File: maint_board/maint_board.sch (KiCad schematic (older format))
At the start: 9 parts, among them J1 USB_mini_micro_B, J2 4P4C, J5 USB_C_Receptacle_USB2.0

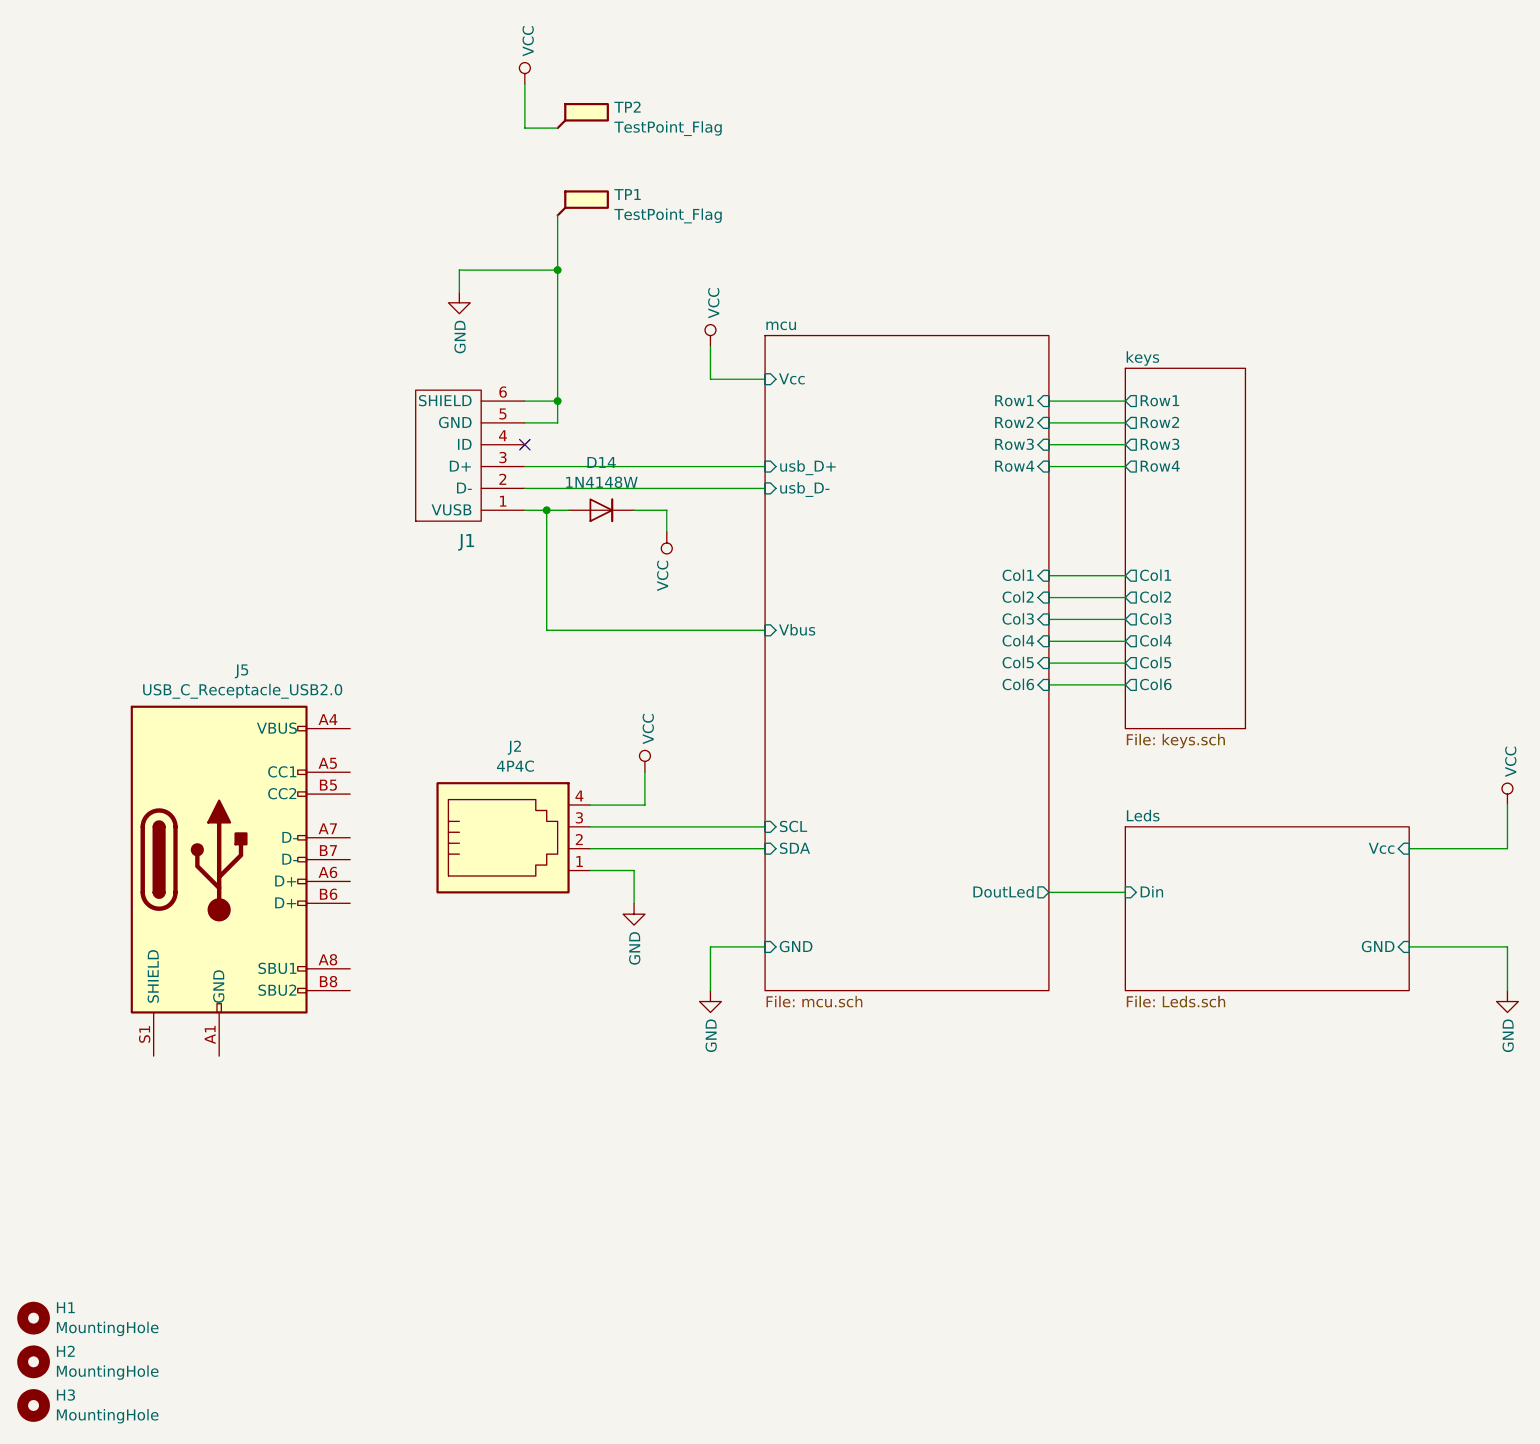
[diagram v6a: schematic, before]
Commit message: added filter on usb shield
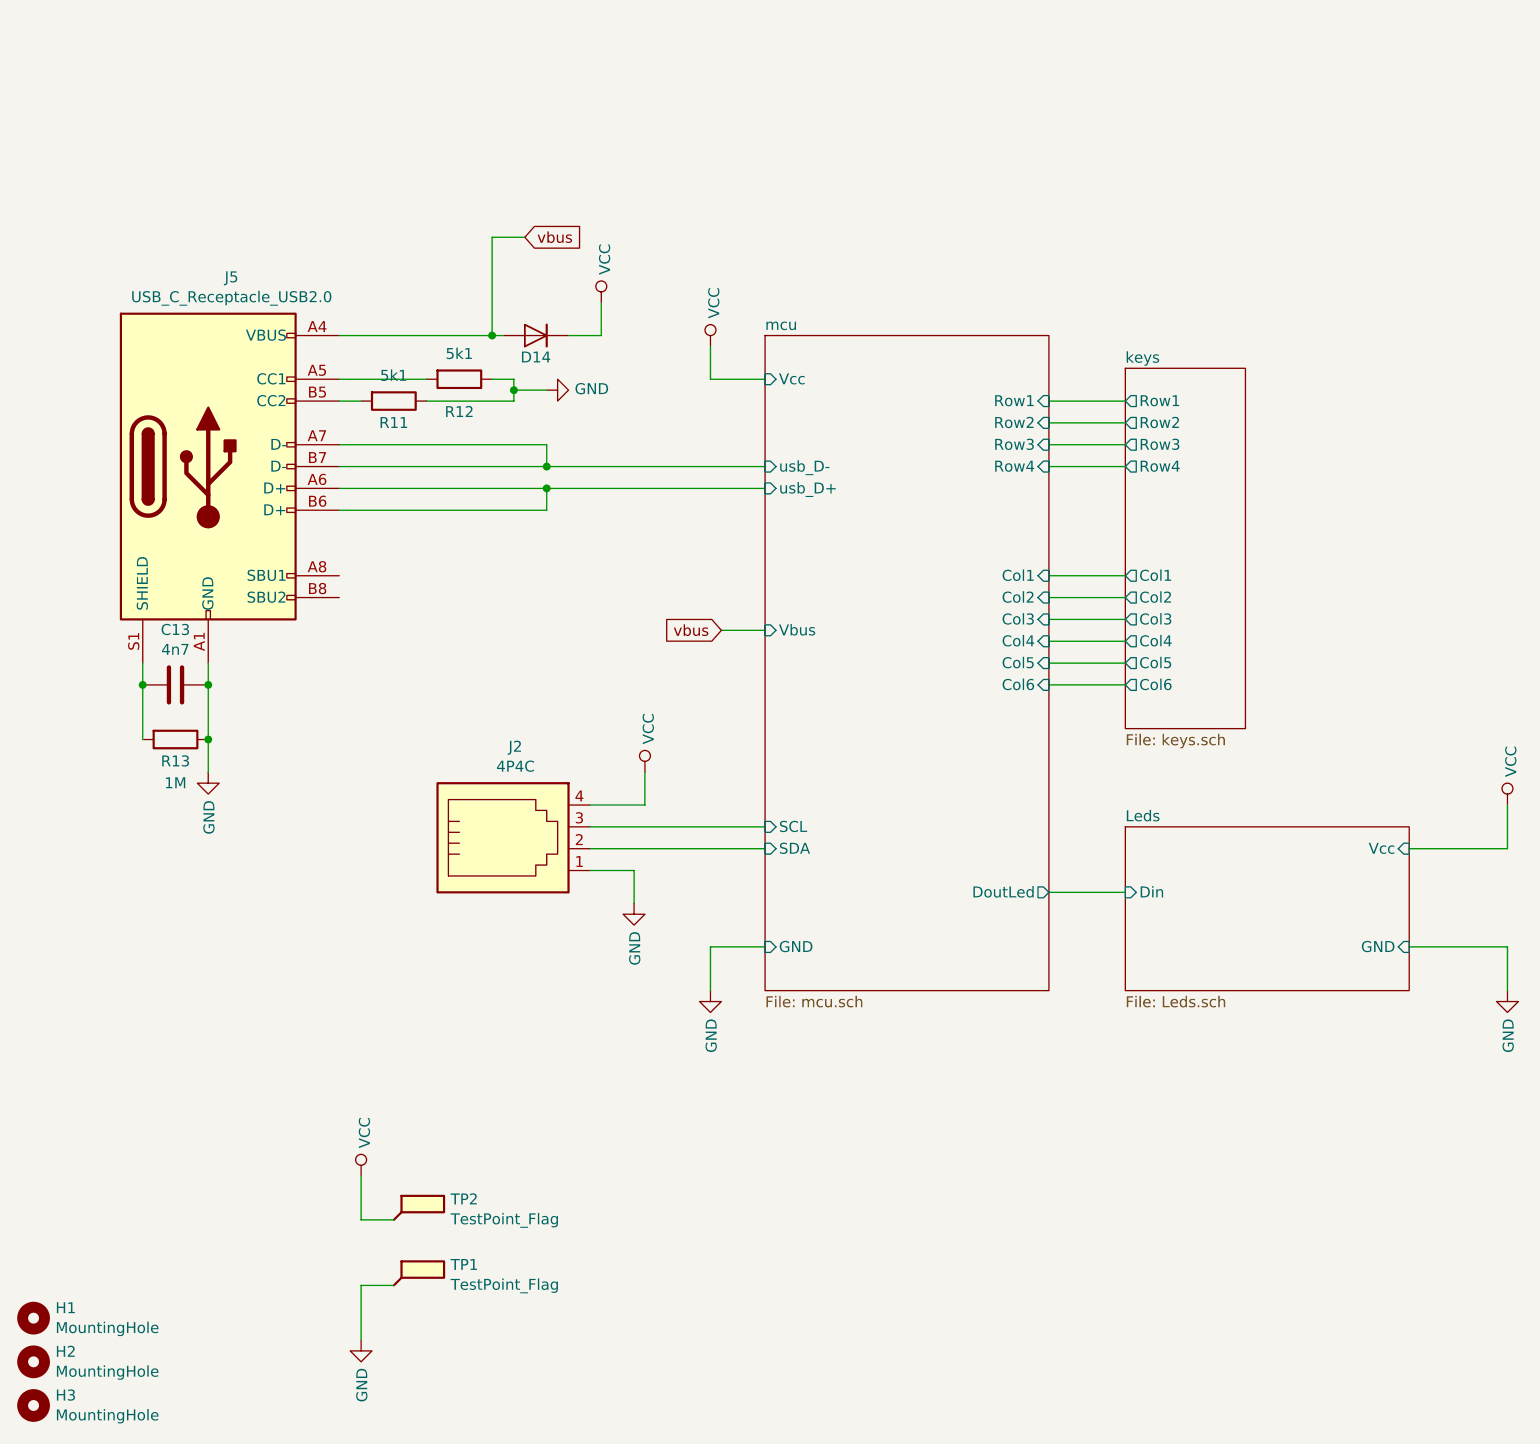
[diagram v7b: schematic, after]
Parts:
- removed J1: USB_mini_micro_B, TB_connectors:usb_minib_wm5462ct-nd, symbol maint_board-rescue:USB_mini_micro_B-keyboard_parts-maint_board-rescue
- added C13: 4n7, keyboard_parts:C_1608, symbol Device:C
- added R11, R12: 5k1, Resistor_SMD:R_0603_1608Metric_Pad1.05x0.95mm_HandSolder, symbol Device:R
- added R13: 1M, Resistor_SMD:R_0603_1608Metric_Pad1.05x0.95mm_HandSolder, symbol Device:R
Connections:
- net mcu/Vbus is gone; now on net vbus: D14.2 (A)
- net GND: now also J5.A1 (GND), J5.A12 (GND), J5.B1 (GND), J5.B12 (GND), C13.1, R11.1, R12.1, R13.1
- net mcu/usb_D+: now also J5.A6 (D+), J5.B6 (D+)
- net mcu/usb_D-: now also J5.A7 (D-), J5.B7 (D-)
- net vbus: now reaches J5.A4 (VBUS), J5.A9 (VBUS), J5.B4 (VBUS), J5.B9 (VBUS)
- net at J5.A5 (CC1): now also R12.2
- net at J5.B5 (CC2): now also R11.2
- net at J5.S1 (SHIELD): now also C13.2, R13.2
- no-connect marks 1 -> 0
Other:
- moved on the sheet: D14, J5, TP1, TP2
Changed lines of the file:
@@
 L power:GND #PWR013
 U 1 1 6050A70E
-P 3000 2250
-F 0 "#PWR013" H 3000 2000 50  0001 C CNN
-F 1 "GND" V 3005 2122 50  0000 R CNN
-F 2 "" H 3000 2250 50  0001 C CNN
-F 3 "" H 3000 2250 50  0001 C CNN
-	1    3000 2250
+P 1850 4450
+F 0 "#PWR013" H 1850 4200 50  0001 C CNN
+F 1 "GND" V 1855 4322 50  0000 R CNN
+F 2 "" H 1850 4450 50  0001 C CNN
+F 3 "" H 1850 4450 50  0001 C CNN
+	1    1850 4450
 	1    0    0    -1
 $EndComp
@@
 L power:VCC #PWR03
 U 1 1 601B611E
-P 3950 3350
-F 0 "#PWR03" H 3950 3200 50  0001 C CNN
-F 1 "VCC" V 3967 3478 50  0000 L CNN
-F 2 "" H 3950 3350 50  0001 C CNN
-F 3 "" H 3950 3350 50  0001 C CNN
-	1    3950 3350
-	-1   0    0    1
-$EndComp
-Wire Wire Line
-	3300 3250 3400 3250
-Wire Wire Line
-	3950 3350 3950 3250
-Wire Wire Line
-	3300 2750 3450 2750
-NoConn ~ 3300 2950
+P 3650 2300
+F 0 "#PWR03" H 3650 2150 50  0001 C CNN
+F 1 "VCC" V 3667 2428 50  0000 L CNN
+F 2 "" H 3650 2300 50  0001 C CNN
+F 3 "" H 3650 2300 50  0001 C CNN
+	1    3650 2300
+	1    0    0    -1
+$EndComp
 Wire Wire Line
 	6050 2750 5700 2750
@@
 F4 "Din" I L 6050 5000 50
 $EndSheet
-Wire Wire Line
-	3300 3050 4400 3050
-Wire Wire Line
-	4400 3150 3300 3150
 $Comp
 L power:VCC #PWR06
@@
 Wire Wire Line
 	5700 5000 6050 5000
-$Comp
-L maint_board-rescue:USB_mini_micro_B-keyboard_parts-maint_board-rescue J1
-U 1 1 601E1AA5
-P 3150 3100
-F 0 "J1" H 3037 3391 60  0000 C CNN
-F 1 "USB_mini_micro_B" H 3000 3350 60  0001 C CNN
-F 2 "TB_connectors:usb_minib_wm5462ct-nd" H 3100 3100 60  0001 C CNN
-F 3 "" H 3100 3100 60  0000 C CNN
-	1    3150 3100
-	1    0    0    1
-$EndComp
-Wire Wire Line
-	3450 2750 3450 2150
-Wire Wire Line
-	3450 2150 3000 2150
-Wire Wire Line
-	3000 2150 3000 2250
-Wire Wire Line
-	3300 2850 3450 2850
-Wire Wire Line
-	3450 2850 3450 2750
-Connection ~ 3450 2750
-Wire Wire Line
-	3800 3250 3950 3250
-Wire Wire Line
-	3400 3250 3400 3800
-Connection ~ 3400 3250
-Wire Wire Line
-	3400 3250 3500 3250
+Wire Wire Line
+	3500 2450 3650 2450
 $Sheet
 S 4400 2450 1300 3000
@@
 F10 "Col5" I R 5700 3950 50
 F11 "Col6" I R 5700 4050 50
-F12 "usb_D-" I L 4400 3150 50
-F13 "usb_D+" I L 4400 3050 50
+F12 "usb_D-" I L 4400 3050 50
+F13 "usb_D+" I L 4400 3150 50
 F14 "Vcc" I L 4400 2650 50
 F15 "GND" I L 4400 5250 50
@@
 $EndSheet
 Wire Wire Line
-	3400 3800 4400 3800
+	4200 3800 4400 3800
 $Comp
 L Diode:1N4148W D14
 U 1 1 61967A26
-P 3650 3250
-F 0 "D14" H 3650 3033 50  0000 C CNN
-F 1 "1N4148W" H 3650 3124 50  0000 C CNN
-F 2 "Diode_SMD:D_SOD-323" H 3650 3075 50  0001 C CNN
-F 3 "https://www.vishay.com/docs/85748/1n4148w.pdf" H 3650 3250 50  0001 C CNN
-	1    3650 3250
+P 3350 2450
+F 0 "D14" H 3350 2550 50  0000 C CNN
+F 1 "1N4148W" H 3350 2700 50  0001 C CNN
+F 2 "Diode_SMD:D_SOD-323" H 3350 2275 50  0001 C CNN
+F 3 "https://www.vishay.com/docs/85748/1n4148w.pdf" H 3350 2450 50  0001 C CNN
+	1    3350 2450
 	-1   0    0    1
 $EndComp
@@
 L Connector:TestPoint_Flag TP1
 U 1 1 61949AE4
-P 3450 1900
-F 0 "TP1" H 3710 1994 50  0000 L CNN
-F 1 "TestPoint_Flag" H 3710 1903 50  0000 L CNN
-F 2 "TestPoint:TestPoint_Pad_1.5x1.5mm" H 3650 1900 50  0001 C CNN
-F 3 "~" H 3650 1900 50  0001 C CNN
-	1    3450 1900
-	1    0    0    -1
-$EndComp
-Wire Wire Line
-	3450 1900 3450 2150
-Connection ~ 3450 2150
+P 2700 6800
+F 0 "TP1" H 2960 6894 50  0000 L CNN
+F 1 "TestPoint_Flag" H 2960 6803 50  0000 L CNN
+F 2 "TestPoint:TestPoint_Pad_1.5x1.5mm" H 2900 6800 50  0001 C CNN
+F 3 "~" H 2900 6800 50  0001 C CNN
+	1    2700 6800
+	1    0    0    -1
+$EndComp
 $Comp
 L Connector:TestPoint_Flag TP2
 U 1 1 619566ED
-P 3450 1500
-F 0 "TP2" H 3710 1594 50  0000 L CNN
-F 1 "TestPoint_Flag" H 3710 1503 50  0000 L CNN
-F 2 "TestPoint:TestPoint_Pad_1.5x1.5mm" H 3650 1500 50  0001 C CNN
-F 3 "~" H 3650 1500 50  0001 C CNN
-	1    3450 1500
+P 2700 6500
+F 0 "TP2" H 2960 6594 50  0000 L CNN
+F 1 "TestPoint_Flag" H 2960 6503 50  0000 L CNN
+F 2 "TestPoint:TestPoint_Pad_1.5x1.5mm" H 2900 6500 50  0001 C CNN
+F 3 "~" H 2900 6500 50  0001 C CNN
+	1    2700 6500
 	1    0    0    -1
 $EndComp
@@
 L power:VCC #PWR038
 U 1 1 6195A3EA
-P 3300 1300
-F 0 "#PWR038" H 3300 1150 50  0001 C CNN
-F 1 "VCC" V 3317 1428 50  0000 L CNN
-F 2 "" H 3300 1300 50  0001 C CNN
-F 3 "" H 3300 1300 50  0001 C CNN
-	1    3300 1300
-	1    0    0    -1
-$EndComp
-Wire Wire Line
-	3450 1500 3300 1500
-Wire Wire Line
-	3300 1500 3300 1300
+P 2550 6300
+F 0 "#PWR038" H 2550 6150 50  0001 C CNN
+F 1 "VCC" V 2567 6428 50  0000 L CNN
+F 2 "" H 2550 6300 50  0001 C CNN
+F 3 "" H 2550 6300 50  0001 C CNN
+	1    2550 6300
+	1    0    0    -1
+$EndComp
+Wire Wire Line
+	2700 6500 2550 6500
+Wire Wire Line
+	2550 6500 2550 6300
 $Comp
 L Connector:USB_C_Receptacle_USB2.0 J5
 U 1 1 61959045
-P 1900 4850
-F 0 "J5" H 2007 5717 50  0000 C CNN
-F 1 "USB_C_Receptacle_USB2.0" H 2007 5626 50  0000 C CNN
-F 2 "Connector_USB:USB_C_Receptacle_Palconn_UTC16-G" H 2050 4850 50  0001 C CNN
-F 3 "https://www.usb.org/sites/default/files/documents/usb_type-c.zip" H 2050 4850 50  0001 C CNN
-	1    1900 4850
-	1    0    0    -1
-$EndComp
+P 1850 3050
+F 0 "J5" H 1957 3917 50  0000 C CNN
+F 1 "USB_C_Receptacle_USB2.0" H 1957 3826 50  0000 C CNN
+F 2 "Connector_USB:USB_C_Receptacle_Palconn_UTC16-G" H 2000 3050 50  0001 C CNN
+F 3 "https://www.usb.org/sites/default/files/documents/usb_type-c.zip" H 2000 3050 50  0001 C CNN
+	1    1850 3050
+	1    0    0    -1
+$EndComp
+Wire Wire Line
+	2450 3150 3400 3150
+Wire Wire Line
+	2450 3250 3400 3250
+Wire Wire Line
+	3400 3250 3400 3150
+Connection ~ 3400 3150
+Wire Wire Line
+	3400 3150 4400 3150
+Wire Wire Line
+	2450 3050 3400 3050
+Wire Wire Line
+	2450 2950 3400 2950
+Wire Wire Line
+	3400 2950 3400 3050
+Connection ~ 3400 3050
+Wire Wire Line
+	3400 3050 4400 3050
+Wire Wire Line
+	3650 2300 3650 2450
+Text GLabel 3300 2000 2    50   Input ~ 0
+vbus
+Text GLabel 4200 3800 0    50   Input ~ 0
+vbus
+Wire Wire Line
+	3300 2000 3150 2000
+Wire Wire Line
+	3150 2000 3150 2450
+Wire Wire Line
+	2450 2450 3150 2450
+Connection ~ 3150 2450
+Wire Wire Line
+	3150 2450 3200 2450
+$Comp
+L power:GND #PWR041
+U 1 1 619CC8E8
+P 2550 7050
+F 0 "#PWR041" H 2550 6800 50  0001 C CNN
+F 1 "GND" V 2555 6922 50  0000 R CNN
+F 2 "" H 2550 7050 50  0001 C CNN
+F 3 "" H 2550 7050 50  0001 C CNN
+	1    2550 7050
+	1    0    0    -1
+$EndComp
+Wire Wire Line
+	2550 7050 2550 6800
+Wire Wire Line
+	2700 6800 2550 6800
+Wire Wire Line
+	1850 3950 1850 4050
+$Comp
+L Device:R R11
+U 1 1 619DA61B
+P 2700 2750
+F 0 "R11" V 2800 2750 50  0000 C CNN
+F 1 "5k1" V 2584 2750 50  0000 C CNN
+F 2 "Resistor_SMD:R_0603_1608Metric_Pad1.05x0.95mm_HandSolder" V 2630 2750 50  0001 C CNN
+F 3 "~" H 2700 2750 50  0001 C CNN
+	1    2700 2750
+	0    1    1    0
+$EndComp
+$Comp
+L Device:R R12
+U 1 1 619DB999
+P 3000 2650
+F 0 "R12" V 3150 2650 50  0000 C CNN
+F 1 "5k1" V 2884 2650 50  0000 C CNN
+F 2 "Resistor_SMD:R_0603_1608Metric_Pad1.05x0.95mm_HandSolder" V 2930 2650 50  0001 C CNN
+F 3 "~" H 3000 2650 50  0001 C CNN
+	1    3000 2650
+	0    1    1    0
+$EndComp
+Wire Wire Line
+	2450 2650 2850 2650
+Wire Wire Line
+	2450 2750 2550 2750
+$Comp
+L power:GND #PWR042
+U 1 1 619E77AB
+P 3400 2700
+F 0 "#PWR042" H 3400 2450 50  0001 C CNN
+F 1 "GND" V 3405 2572 50  0000 R CNN
+F 2 "" H 3400 2700 50  0001 C CNN
+F 3 "" H 3400 2700 50  0001 C CNN
+	1    3400 2700
+	0    -1   -1   0
+$EndComp
+Wire Wire Line
+	3150 2650 3250 2650
+Wire Wire Line
+	3250 2650 3250 2700
+Wire Wire Line
+	2850 2750 3250 2750
+Wire Wire Line
+	3400 2700 3250 2700
+Connection ~ 3250 2700
+Wire Wire Line
+	3250 2700 3250 2750
+$Comp
+L Device:R R13
+U 1 1 619ED292
+P 1700 4300
+F 0 "R13" V 1800 4300 50  0000 C CNN
+F 1 "1M" V 1900 4300 50  0000 C CNN
+F 2 "Resistor_SMD:R_0603_1608Metric_Pad1.05x0.95mm_HandSolder" V 1630 4300 50  0001 C CNN
+F 3 "~" H 1700 4300 50  0001 C CNN
+	1    1700 4300
+	0    1    1    0
+$EndComp
+$Comp
+L Device:C C13
+U 1 1 619ED8D8
+P 1700 4050
+F 0 "C13" V 1448 4050 50  0000 C CNN
+F 1 "4n7" V 1539 4050 50  0000 C CNN
+F 2 "keyboard_parts:C_1608" H 1738 3900 50  0001 C CNN
+F 3 "~" H 1700 4050 50  0001 C CNN
+	1    1700 4050
+	0    1    1    0
+$EndComp
+Connection ~ 1850 4050
+Wire Wire Line
+	1850 4050 1850 4300
+Connection ~ 1850 4300
+Wire Wire Line
+	1850 4300 1850 4450
+Wire Wire Line
+	1550 3950 1550 4050
+Connection ~ 1550 4050
+Wire Wire Line
+	1550 4050 1550 4300
 $EndSCHEMATC

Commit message: added som libes
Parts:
- TP1: value TestPoint_Flag -> gnd
- TP2: value TestPoint_Flag -> Vcc
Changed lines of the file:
@@
 P 2700 6800
 F 0 "TP1" H 2960 6894 50  0000 L CNN
-F 1 "TestPoint_Flag" H 2960 6803 50  0000 L CNN
+F 1 "gnd" H 2960 6803 50  0000 L CNN
 F 2 "TestPoint:TestPoint_Pad_1.5x1.5mm" H 2900 6800 50  0001 C CNN
 F 3 "~" H 2900 6800 50  0001 C CNN
@@
 P 2700 6500
 F 0 "TP2" H 2960 6594 50  0000 L CNN
-F 1 "TestPoint_Flag" H 2960 6503 50  0000 L CNN
+F 1 "Vcc" H 2960 6503 50  0000 L CNN
 F 2 "TestPoint:TestPoint_Pad_1.5x1.5mm" H 2900 6500 50  0001 C CNN
 F 3 "~" H 2900 6500 50  0001 C CNN
